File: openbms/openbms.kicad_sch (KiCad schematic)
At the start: 0 parts

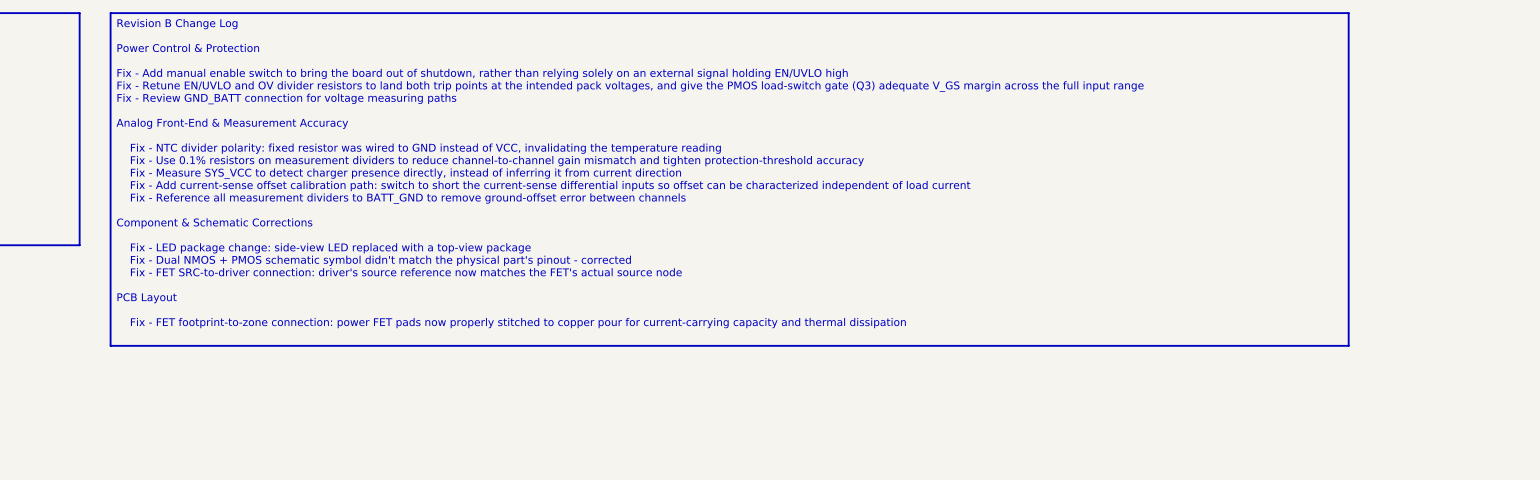
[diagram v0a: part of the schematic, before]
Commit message: Teardrops added, EEPROM part number updated, production files released
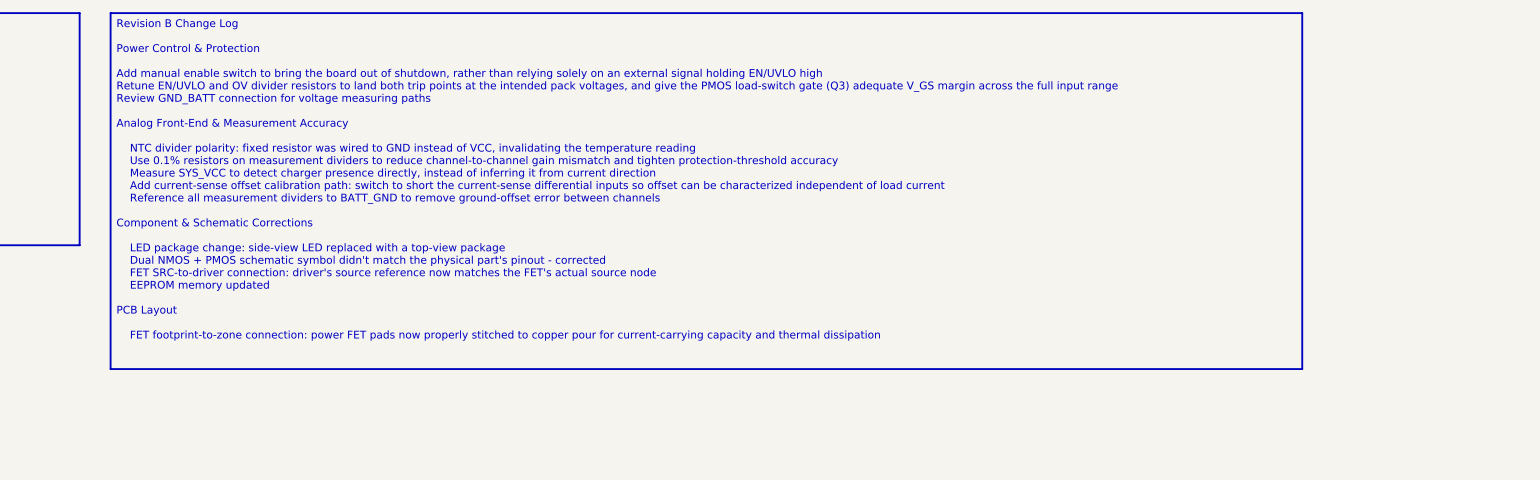
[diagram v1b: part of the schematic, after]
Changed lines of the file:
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@@
 		)
 	)
-	(text_box "Revision B Change Log\n\nPower Control & Protection\n\n    Fix - Add manual enable switch to bring the board out of shutdown, rather than relying solely on an external signal holding EN/UVLO high\n    Fix - Retune EN/UVLO and OV divider resistors to land both trip points at the intended pack voltages, and give the PMOS load-switch gate (Q3) adequate V_GS margin across the full input range\n    Fix - Review GND_BATT connection for voltage measuring paths\n\nAnalog Front-End & Measurement Accuracy\n\n	Fix - NTC divider polarity: fixed resistor was wired to GND instead of VCC, invalidating the temperature reading\n	Fix - Use 0.1% resistors on measurement dividers to reduce channel-to-channel gain mismatch and tighten protection-threshold accuracy\n	Fix - Measure SYS_VCC to detect charger presence directly, instead of inferring it from current direction\n	Fix - Add current-sense offset calibration path: switch to short the current-sense differential inputs so offset can be characterized independent of load current\n	Fix - Reference all measurement dividers to BATT_GND to remove ground-offset error between channels\n\nComponent & Schematic Corrections\n\n	Fix - LED package change: side-view LED replaced with a top-view package\n	Fix - Dual NMOS + PMOS schematic symbol didn't match the physical part's pinout - corrected\n	Fix - FET SRC-to-driver connection: driver's source reference now matches the FET's actual source node\n\nPCB Layout\n\n	Fix - FET footprint-to-zone connection: power FET pads now properly stitched to copper pour for current-carrying capacity and thermal dissipation"
+	(text_box "Revision B Change Log\n\nPower Control & Protection\n\n    Add manual enable switch to bring the board out of shutdown, rather than relying solely on an external signal holding EN/UVLO high\n    Retune EN/UVLO and OV divider resistors to land both trip points at the intended pack voltages, and give the PMOS load-switch gate (Q3) adequate V_GS margin across the full input range\n    Review GND_BATT connection for voltage measuring paths\n\nAnalog Front-End & Measurement Accuracy\n\n	NTC divider polarity: fixed resistor was wired to GND instead of VCC, invalidating the temperature reading\n	Use 0.1% resistors on measurement dividers to reduce channel-to-channel gain mismatch and tighten protection-threshold accuracy\n	Measure SYS_VCC to detect charger presence directly, instead of inferring it from current direction\n	Add current-sense offset calibration path: switch to short the current-sense differential inputs so offset can be characterized independent of load current\n	Reference all measurement dividers to BATT_GND to remove ground-offset error between channels\n\nComponent & Schematic Corrections\n\n	LED package change: side-view LED replaced with a top-view package\n	Dual NMOS + PMOS schematic symbol didn't match the physical part's pinout - corrected\n	FET SRC-to-driver connection: driver's source reference now matches the FET's actual source node\n	EEPROM memory updated\n\nPCB Layout\n\n	FET footprint-to-zone connection: power FET pads now properly stitched to copper pour for current-carrying capacity and thermal dissipation"
 		(exclude_from_sim no)
 		(at 139.7 17.78 0)
-		(size 203.2 54.61)
+		(size 195.58 58.42)
 		(margins 0.9525 0.9525 0.9525 0.9525)
 		(stroke
